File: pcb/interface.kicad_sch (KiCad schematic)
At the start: 1 part, among them J2 Conn_01x06_Pin

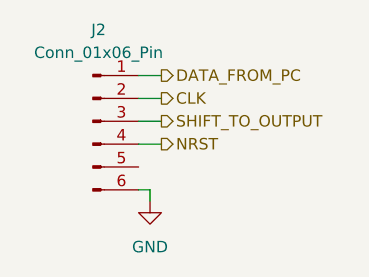
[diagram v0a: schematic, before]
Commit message: Add output LED array
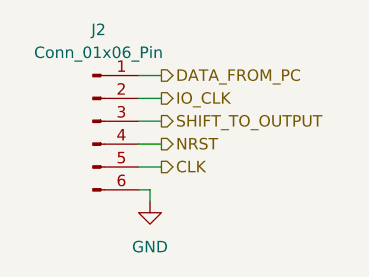
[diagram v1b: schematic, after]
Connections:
- net CLK: now also J2.5 (Pin_5); no longer J2.2 (Pin_2)
- new net IO_CLK: J2.2 (Pin_2)
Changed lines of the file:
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@@
+	(wire
+		(pts
+			(xy 121.92 95.25) (xy 124.46 95.25)
+		)
+		(stroke
+			(width 0)
+			(type default)
+		)
+	)
 	(wire
 		(pts
@@
 		)
 	)
-	(hierarchical_label "CLK"
+	(hierarchical_label "IO_CLK"
 		(shape output)
 		(at 124.46 87.63 0)
 		(effects
 			(font
+				(size 1.27 1.27)
+			)
+			(justify left)
+		)
+	)
+	(hierarchical_label "CLK"
+		(shape output)
+		(at 124.46 95.25 0)
+		(effects
+			(font
